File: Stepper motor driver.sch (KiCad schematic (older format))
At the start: 14 parts

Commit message: finished schematic, started PCB routing
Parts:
- removed Q? (x4): BD237, TO-126, symbol BD237
- added Q1, Q2, Q3, Q4: TIP120, Power_Integrations:TO-220, symbol TIP120
- added W1, W2, W3, W4, W5, W6, W7, W8: TEST_1P, Measurement_Points:Measurement_Point_Round-TH_Big, symbol TEST_1P
- D1, D2, D3, D4: renamed from D?; value D -> 1N4003; footprint (none) -> Diodes_ThroughHole:Diode_DO-41_SOD81_Horizontal_RM10
- R1, R2, R3, R4: renamed from R?; value R -> 180; footprint (none) -> Resistors_ThroughHole:Resistor_Horizontal_RM10mm
- U1, U2: renamed from U?; footprint (none) -> Housings_DIP:DIP-16_W7.62mm_LongPads
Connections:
- net labels added: CLK
- net labels removed: STEP, Wire_1, Wire_2, Wire_3, Wire_4, Wire_5, Wire_6

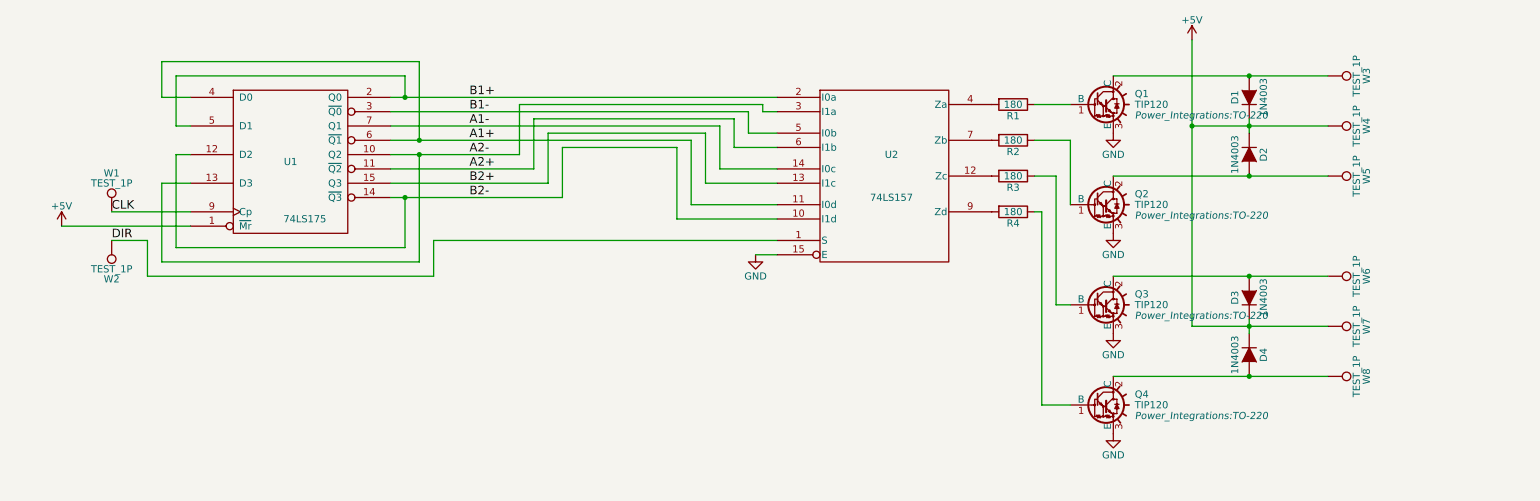
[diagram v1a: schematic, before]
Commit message: fixed schematic and finished all routing
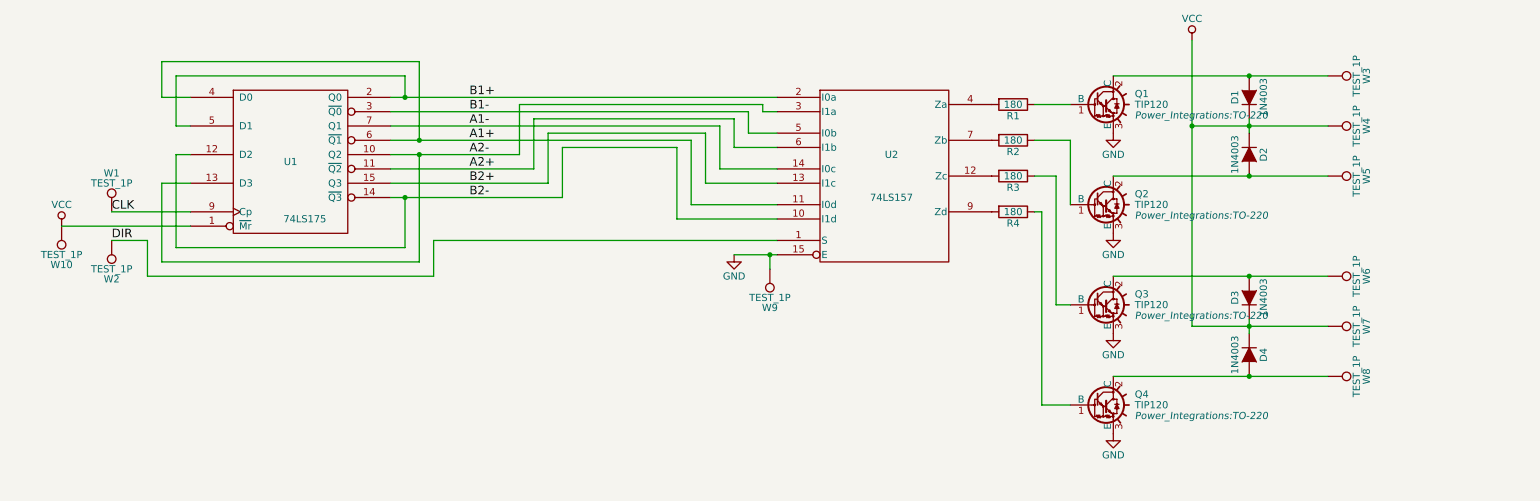
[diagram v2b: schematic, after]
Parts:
- added W10, W9: TEST_1P, Measurement_Points:Measurement_Point_Round-TH_Big, symbol TEST_1P
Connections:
- net +5V is gone; now on net VCC: D1.1 (K), D2.1 (K), D3.1 (K), D4.1 (K), U1.1 (~Mr), W4.1, W7.1
- net GND: now also W9.1
- net VCC: now also W10.1
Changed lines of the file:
@@
 Wire Wire Line
 	5150 4300 5850 4300
-$Comp
-L +5V #PWR01
-U 1 1 571E9B86
-P 850 4350
-F 0 "#PWR01" H 850 4200 50  0001 C CNN
-F 1 "+5V" H 850 4490 50  0000 C CNN
-F 2 "" H 850 4350 50  0000 C CNN
-F 3 "" H 850 4350 50  0000 C CNN
-	1    850  4350
-	1    0    0    -1
-$EndComp
 Wire Wire Line
 	1750 4350 850  4350
@@
 $EndComp
 $Comp
-L GND #PWR02
+L GND #PWR01
 U 1 1 571F00C5
 P 8200 4400
-F 0 "#PWR02" H 8200 4150 50  0001 C CNN
+F 0 "#PWR01" H 8200 4150 50  0001 C CNN
 F 1 "GND" H 8200 4250 50  0000 C CNN
 F 2 "" H 8200 4400 50  0000 C CNN
@@
 	5850 4450 3450 4450
 $Comp
-L GND #PWR03
+L GND #PWR02
 U 1 1 5721DF02
 P 8200 5100
-F 0 "#PWR03" H 8200 4850 50  0001 C CNN
+F 0 "#PWR02" H 8200 4850 50  0001 C CNN
 F 1 "GND" H 8200 4950 50  0000 C CNN
 F 2 "" H 8200 5100 50  0000 C CNN
@@
 $EndComp
 $Comp
-L GND #PWR04
+L GND #PWR03
 U 1 1 5721DF69
 P 8200 5800
-F 0 "#PWR04" H 8200 5550 50  0001 C CNN
+F 0 "#PWR03" H 8200 5550 50  0001 C CNN
 F 1 "GND" H 8200 5650 50  0000 C CNN
 F 2 "" H 8200 5800 50  0000 C CNN
@@
 $EndComp
 $Comp
-L +5V #PWR05
-U 1 1 5721E04E
-P 8750 3050
-F 0 "#PWR05" H 8750 2900 50  0001 C CNN
-F 1 "+5V" H 8750 3190 50  0000 C CNN
-F 2 "" H 8750 3050 50  0000 C CNN
-F 3 "" H 8750 3050 50  0000 C CNN
-	1    8750 3050
-	1    0    0    -1
-$EndComp
-$Comp
-L GND #PWR06
+L GND #PWR04
 U 1 1 5721E209
 P 8200 3700
-F 0 "#PWR06" H 8200 3450 50  0001 C CNN
+F 0 "#PWR04" H 8200 3450 50  0001 C CNN
 F 1 "GND" H 8200 3550 50  0000 C CNN
 F 2 "" H 8200 3700 50  0000 C CNN
@@
 $EndComp
 $Comp
-L GND #PWR07
+L GND #PWR05
 U 1 1 57227721
-P 5700 4550
-F 0 "#PWR07" H 5700 4300 50  0001 C CNN
-F 1 "GND" H 5700 4400 50  0000 C CNN
-F 2 "" H 5700 4550 50  0000 C CNN
-F 3 "" H 5700 4550 50  0000 C CNN
-	1    5700 4550
-	1    0    0    -1
-$EndComp
-Wire Wire Line
-	5700 4550 5850 4550
+P 5550 4550
+F 0 "#PWR05" H 5550 4300 50  0001 C CNN
+F 1 "GND" H 5550 4400 50  0000 C CNN
+F 2 "" H 5550 4550 50  0000 C CNN
+F 3 "" H 5550 4550 50  0000 C CNN
+	1    5550 4550
+	1    0    0    -1
+$EndComp
+Wire Wire Line
+	5550 4550 5850 4550
 $Comp
 L TEST_1P W6
@@
 Text Label 1200 4250 0    60   ~ 0
 CLK
+$Comp
+L VCC #PWR06
+U 1 1 572404FF
+P 850 4350
+F 0 "#PWR06" H 850 4200 50  0001 C CNN
+F 1 "VCC" H 850 4500 50  0000 C CNN
+F 2 "" H 850 4350 50  0000 C CNN
+F 3 "" H 850 4350 50  0000 C CNN
+	1    850  4350
+	1    0    0    -1
+$EndComp
+$Comp
+L VCC #PWR07
+U 1 1 57240D11
+P 8750 3050
+F 0 "#PWR07" H 8750 2900 50  0001 C CNN
+F 1 "VCC" H 8750 3200 50  0000 C CNN
+F 2 "" H 8750 3050 50  0000 C CNN
+F 3 "" H 8750 3050 50  0000 C CNN
+	1    8750 3050
+	1    0    0    -1
+$EndComp
+$Comp
+L TEST_1P W10
+U 1 1 57241938
+P 850 4350
+F 0 "W10" H 850 4620 50  0000 C CNN
+F 1 "TEST_1P" H 850 4550 50  0000 C CNN
+F 2 "Measurement_Points:Measurement_Point_Round-TH_Big" H 1050 4350 50  0001 C CNN
+F 3 "" H 1050 4350 50  0000 C CNN
+	1    850  4350
+	-1   0    0    1
+$EndComp
+$Comp
+L TEST_1P W9
+U 1 1 57241B12
+P 5800 4650
+F 0 "W9" H 5800 4920 50  0000 C CNN
+F 1 "TEST_1P" H 5800 4850 50  0000 C CNN
+F 2 "Measurement_Points:Measurement_Point_Round-TH_Big" H 6000 4650 50  0001 C CNN
+F 3 "" H 6000 4650 50  0000 C CNN
+	1    5800 4650
+	-1   0    0    1
+$EndComp
+Wire Wire Line
+	5800 4650 5800 4550
+Connection ~ 5800 4550
 $EndSCHEMATC

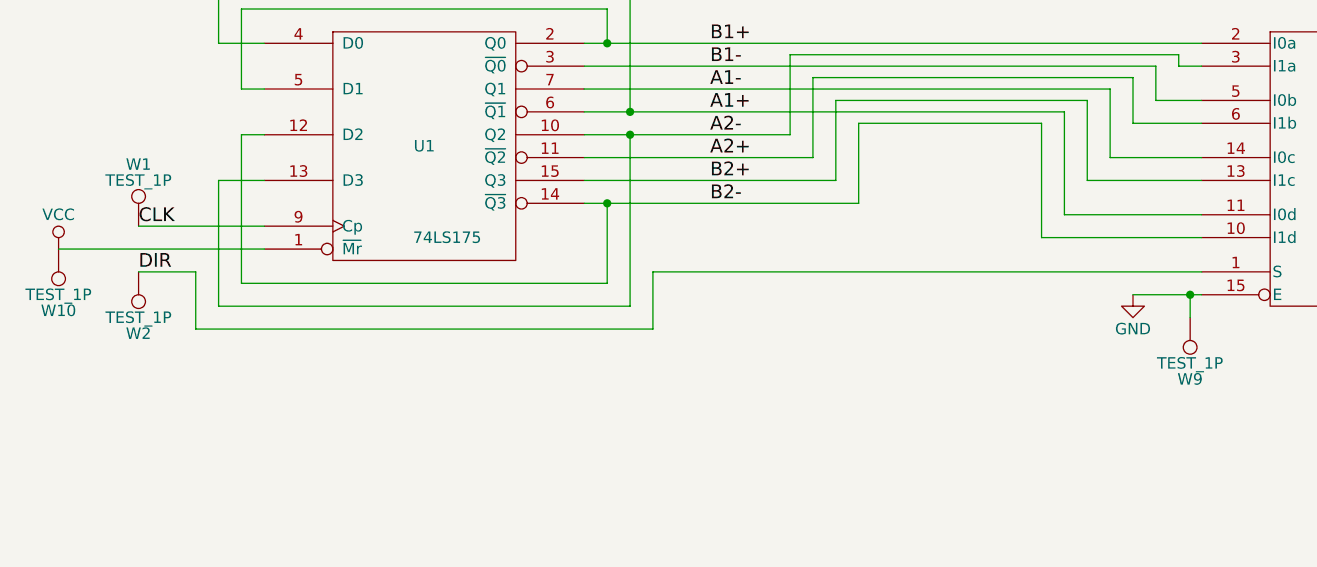
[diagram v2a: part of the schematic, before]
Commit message: touched up schematic and PCB, added ground pour, updated gerber and image files
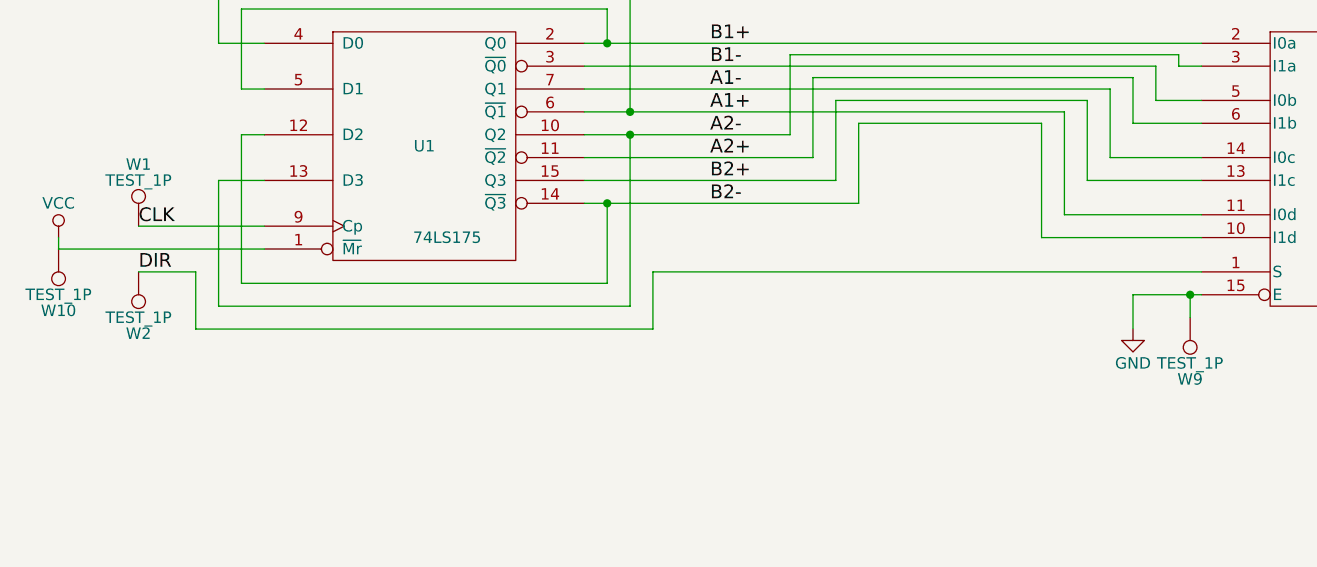
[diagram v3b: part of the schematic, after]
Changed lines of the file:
@@
 L GND #PWR05
 U 1 1 57227721
-P 5550 4550
-F 0 "#PWR05" H 5550 4300 50  0001 C CNN
-F 1 "GND" H 5550 4400 50  0000 C CNN
-F 2 "" H 5550 4550 50  0000 C CNN
-F 3 "" H 5550 4550 50  0000 C CNN
-	1    5550 4550
+P 5550 4700
+F 0 "#PWR05" H 5550 4450 50  0001 C CNN
+F 1 "GND" H 5550 4550 50  0000 C CNN
+F 2 "" H 5550 4700 50  0000 C CNN
+F 3 "" H 5550 4700 50  0000 C CNN
+	1    5550 4700
 	1    0    0    -1
 $EndComp
@@
 L VCC #PWR06
 U 1 1 572404FF
-P 850 4350
-F 0 "#PWR06" H 850 4200 50  0001 C CNN
-F 1 "VCC" H 850 4500 50  0000 C CNN
-F 2 "" H 850 4350 50  0000 C CNN
-F 3 "" H 850 4350 50  0000 C CNN
-	1    850  4350
+P 850 4300
+F 0 "#PWR06" H 850 4150 50  0001 C CNN
+F 1 "VCC" H 850 4450 50  0000 C CNN
+F 2 "" H 850 4300 50  0000 C CNN
+F 3 "" H 850 4300 50  0000 C CNN
+	1    850  4300
 	1    0    0    -1
 $EndComp
@@
 	5800 4650 5800 4550
 Connection ~ 5800 4550
+Wire Wire Line
+	850  4350 850  4300
+Wire Wire Line
+	5550 4700 5550 4550
 $EndSCHEMATC

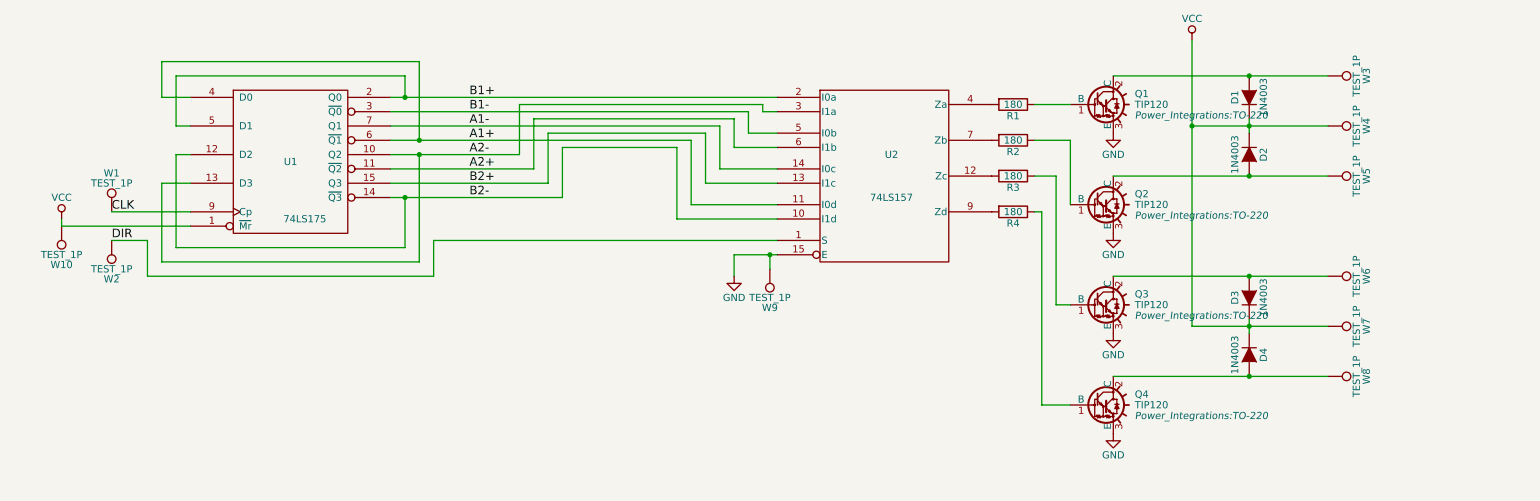
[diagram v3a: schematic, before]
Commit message: Added connectors for I/O and changed to SMD components
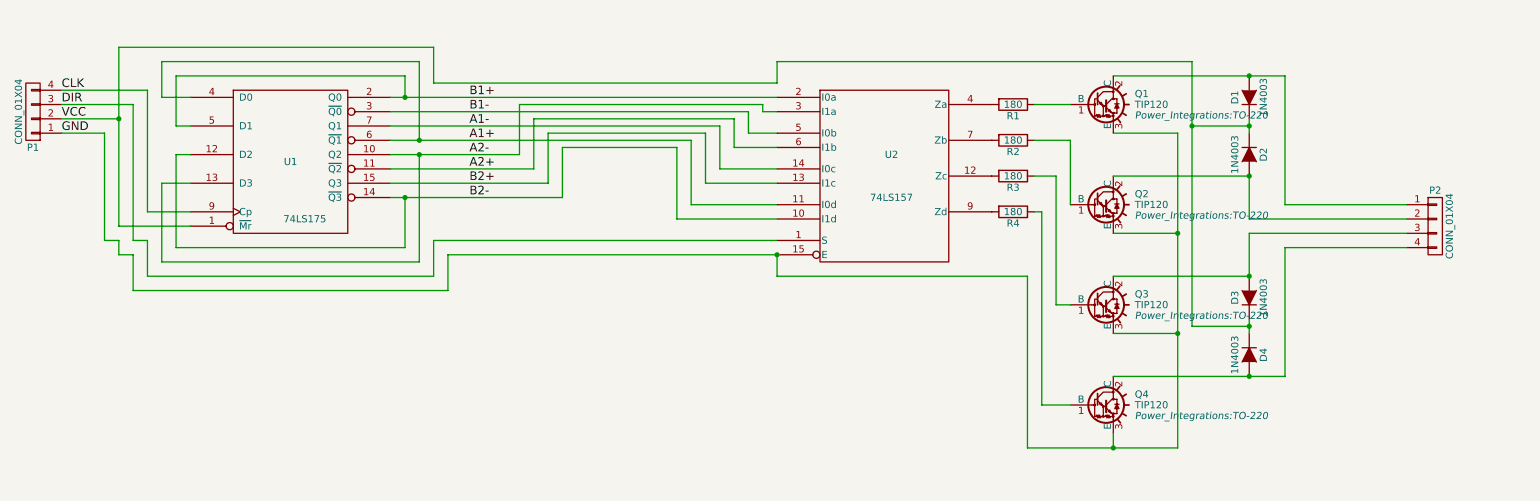
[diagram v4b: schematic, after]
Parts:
- removed W1, W10, W2, W3, W4, W5, W6, W7, W8, W9: TEST_1P, Measurement_Points:Measurement_Point_Round-TH_Big, symbol TEST_1P
- added P1, P2: CONN_01X04, Connect:Grove_1x04, symbol CONN_01X04
- D1, D2, D3, D4: footprint Diodes_ThroughHole:Diode_DO-41_SOD81_Horizontal_RM10 -> Diodes_ThroughHole:D_DO-35_SOD27_P7.62mm_Horizontal
- R1, R2, R3, R4: footprint Resistors_ThroughHole:Resistor_Horizontal_RM10mm -> Resistors_SMD:R_1206_HandSoldering
- U1, U2: footprint Housings_DIP:DIP-16_W7.62mm_LongPads -> SMD_Packages:SO-16-N
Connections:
- net CLK: now also P1.4 (P4)
- net DIR: now also P1.3 (P3)
- net GND: now also P1.1 (P1)
- net VCC: now also P1.2 (P2)
- net at D1.2 (A), Q1.2 (C): now also P2.1 (P1)
- net at D2.2 (A), Q2.2 (C): now also P2.2 (P2)
- net at D3.2 (A), Q3.2 (C): now also P2.3 (P3)
- net at D4.2 (A), Q4.2 (C): now also P2.4 (P4)
